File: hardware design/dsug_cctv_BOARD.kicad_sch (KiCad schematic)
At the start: 54 parts, among them J1 Conn_02x05_Top_Bottom, J3 TYPEC-304-ACP16, SW1 TS-1187A-B-A-B, SW2 24_detent, SW3 SW_Push, U1 AMS1117-3.3, U13 RP2040, U15 AP63205WU, U16 74AHCT1G125, U2 W25Q128JVS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

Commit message: minor pcb changes
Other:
- moved on the sheet: C56
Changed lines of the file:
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@@
 	)
 	(junction
-		(at 80.01 257.81)
-		(diameter 0)
-		(color 0 0 0 0)
-	)
-	(junction
 		(at 364.236 207.264)
 		(diameter 0)
@@
 	)
 	(junction
-		(at 93.98 270.51)
-		(diameter 0)
-		(color 0 0 0 0)
-	)
-	(junction
 		(at 167.132 258.826)
 		(diameter 0)
@@
 	(wire
 		(pts
-			(xy 80.01 267.97) (xy 80.01 270.51)
+			(xy 242.57 107.188) (xy 230.632 107.188)
 		)
 		(stroke
@@
 	(wire
 		(pts
-			(xy 242.57 107.188) (xy 230.632 107.188)
+			(xy 135.89 200.66) (xy 123.19 200.66)
 		)
 		(stroke
@@
 	(wire
 		(pts
-			(xy 80.01 270.51) (xy 93.98 270.51)
-		)
-		(stroke
-			(width 0)
-			(type default)
-		)
-	)
-	(wire
-		(pts
 			(xy 293.624 211.328) (xy 293.624 209.296)
 		)
@@
 	(wire
 		(pts
+			(xy 135.89 203.2) (xy 135.89 200.66)
+		)
+		(stroke
+			(width 0)
+			(type default)
+		)
+	)
+	(wire
+		(pts
 			(xy 341.376 184.912) (xy 339.598 184.912)
 		)
@@
 	(wire
 		(pts
+			(xy 135.89 214.63) (xy 135.89 210.82)
+		)
+		(stroke
+			(width 0)
+			(type default)
+		)
+	)
+	(wire
+		(pts
 			(xy 143.51 258.826) (xy 155.702 258.826)
 		)
@@
 	(wire
 		(pts
-			(xy 80.01 257.81) (xy 80.01 260.35)
-		)
-		(stroke
-			(width 0)
-			(type default)
-		)
-	)
-	(wire
-		(pts
 			(xy 118.11 200.66) (xy 115.57 200.66)
 		)
@@
 	(symbol
 		(lib_id "Device:C_Polarized_US")
-		(at 80.01 264.16 0)
+		(at 135.89 207.01 0)
 		(unit 1)
 		(exclude_from_sim no)
@@
 		(fields_autoplaced yes)
 		(property "Reference" "C56"
-			(at 83.82 262.2549 0)
+			(at 139.7 205.1049 0)
 			(effects
 				(font
@@
 		)
 		(property "Value" "22uF"
-			(at 83.82 264.7949 0)
+			(at 139.7 207.6449 0)
 			(effects
 				(font
@@
 		)
 		(property "Footprint" "Capacitor_THT:CP_Radial_D5.0mm_P2.50mm"
-			(at 80.01 264.16 0)
+			(at 135.89 207.01 0)
 			(effects
 				(font
@@
 		)
 		(property "Datasheet" "~"
-			(at 80.01 264.16 0)
+			(at 135.89 207.01 0)
 			(effects
 				(font
@@
 		)
 		(property "Description" ""
-			(at 80.01 264.16 0)
+			(at 135.89 207.01 0)
 			(effects
 				(font
@@
 					(unit 1)
 				)
+			)
+		)
+	)
+	(symbol
+		(lib_name "GND_1")
+		(lib_id "power:GND")
+		(at 135.89 214.63 0)
+		(unit 1)
+		(exclude_from_sim no)
+		(in_bom yes)
+		(on_board yes)
+		(dnp no)
+		(fields_autoplaced yes)
+		(property "Reference" "#PWR076"
+			(at 135.89 220.98 0)
+			(effects
+				(font
+					(size 1.27 1.27)
+				)
+				(hide yes)
+			)
+		)
+		(property "Value" "GND"
+			(at 135.89 219.71 0)
+			(effects
+				(font
+					(size 1.27 1.27)
+				)
+			)
+		)
+		(property "Footprint" ""
+			(at 135.89 214.63 0)
+			(effects
+				(font
+					(size 1.27 1.27)
+				)
+				(hide yes)
+			)
+		)
+		(property "Datasheet" ""
+			(at 135.89 214.63 0)
+			(effects
+				(font
+					(size 1.27 1.27)
+				)
+				(hide yes)
+			)
+		)
+		(property "Description" "Power symbol creates a global label with name \"GND\" , ground"
+			(at 135.89 214.63 0)
+			(effects
+				(font
+					(size 1.27 1.27)
+				)
+				(hide yes)
+			)
+		)
+		(pin "1"
+		)
+		(instances
+			(project "dsug_cctv_BOARD"
+				(path "/51d56f2e-5cbb-4b7a-b5cc-91fdc3a7308d"
+					(reference "#PWR076")
+					(unit 1)
+				)

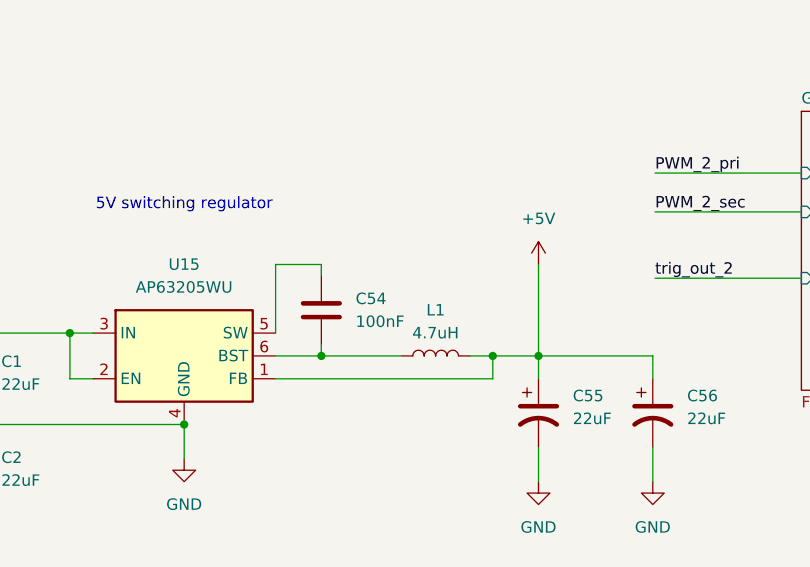
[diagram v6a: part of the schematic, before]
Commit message: switched pin that inductor on buck recitifier is connected to
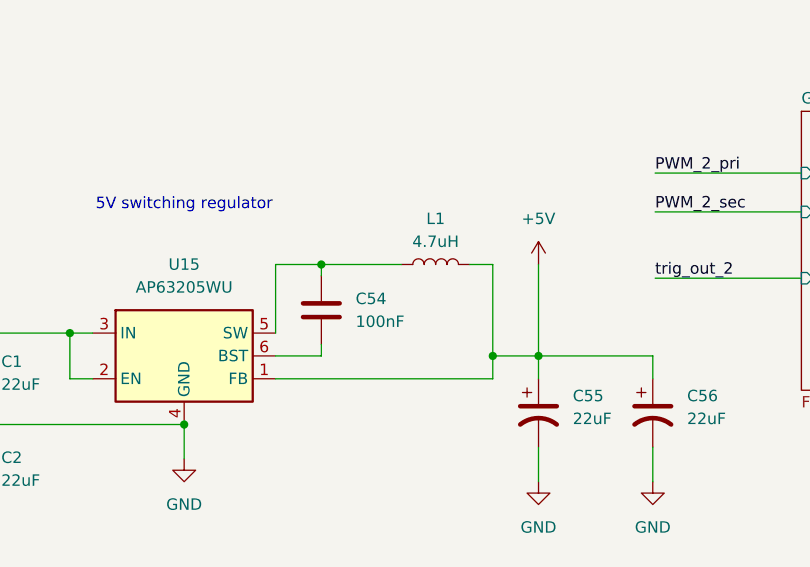
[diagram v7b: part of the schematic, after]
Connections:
- net at C54.1, U15.5 (SW): now also L1.1
- net at C54.2, U15.6 (BST): no longer L1.1
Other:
- moved on the sheet: L1
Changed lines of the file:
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@@
 	)
 	(junction
-		(at 99.06 200.66)
-		(diameter 0)
-		(color 0 0 0 0)
-	)
-	(junction
 		(at 199.898 258.826)
 		(diameter 0)
@@
 	)
 	(junction
+		(at 99.06 190.5)
+		(diameter 0)
+		(color 0 0 0 0)
+	)
+	(junction
 		(at 107.95 257.81)
 		(diameter 0)
@@
 	(wire
 		(pts
-			(xy 99.06 190.5) (xy 99.06 191.77)
-		)
-		(stroke
-			(width 0)
-			(type default)
-		)
-	)
-	(wire
-		(pts
 			(xy 198.374 60.452) (xy 199.898 60.452)
 		)
@@
 	(wire
 		(pts
+			(xy 99.06 199.39) (xy 99.06 200.66)
+		)
+		(stroke
+			(width 0)
+			(type default)
+		)
+	)
+	(wire
+		(pts
 			(xy 135.89 203.2) (xy 135.89 200.66)
 		)
@@
 	(wire
 		(pts
-			(xy 99.06 200.66) (xy 107.95 200.66)
+			(xy 99.06 190.5) (xy 107.95 190.5)
 		)
 		(stroke
@@
 	(wire
 		(pts
+			(xy 118.11 190.5) (xy 118.11 200.66)
+		)
+		(stroke
+			(width 0)
+			(type default)
+		)
+	)
+	(wire
+		(pts
 			(xy 184.912 175.006) (xy 205.232 175.006)
 		)
@@
 	(wire
 		(pts
-			(xy 99.06 199.39) (xy 99.06 200.66)
-		)
-		(stroke
-			(width 0)
-			(type default)
-		)
-	)
-	(wire
-		(pts
 			(xy 323.342 174.752) (xy 315.214 174.752)
 		)
@@
 	(wire
 		(pts
-			(xy 118.11 200.66) (xy 115.57 200.66)
+			(xy 118.11 190.5) (xy 115.57 190.5)
 		)
 		(stroke
@@
 	(wire
 		(pts
+			(xy 99.06 190.5) (xy 99.06 191.77)
+		)
+		(stroke
+			(width 0)
+			(type default)
+		)
+	)
+	(wire
+		(pts
 			(xy 242.57 167.386) (xy 230.632 167.386)
 		)
@@
 	(symbol
 		(lib_id "Device:L")
-		(at 111.76 200.66 90)
+		(at 111.76 190.5 90)
 		(unit 1)
 		(exclude_from_sim no)
@@
 		(fields_autoplaced yes)
 		(property "Reference" "L1"
-			(at 111.76 195.58 90)
+			(at 111.76 185.42 90)
 			(effects
 				(font
@@
 		)
 		(property "Value" "4.7uH"
-			(at 111.76 198.12 90)
+			(at 111.76 187.96 90)
 			(effects
 				(font
@@
 		)
 		(property "Footprint" "User_Footprints:L_TaiTech_HPC3010TF-4R7M"
-			(at 111.76 200.66 0)
+			(at 111.76 190.5 0)
 			(effects
 				(font
@@
 		)
 		(property "Datasheet" "~"
-			(at 111.76 200.66 0)
+			(at 111.76 190.5 0)
 			(effects
 				(font
@@
 		)
 		(property "Description" "Inductor"
-			(at 111.76 200.66 0)
+			(at 111.76 190.5 0)
 			(effects
 				(font

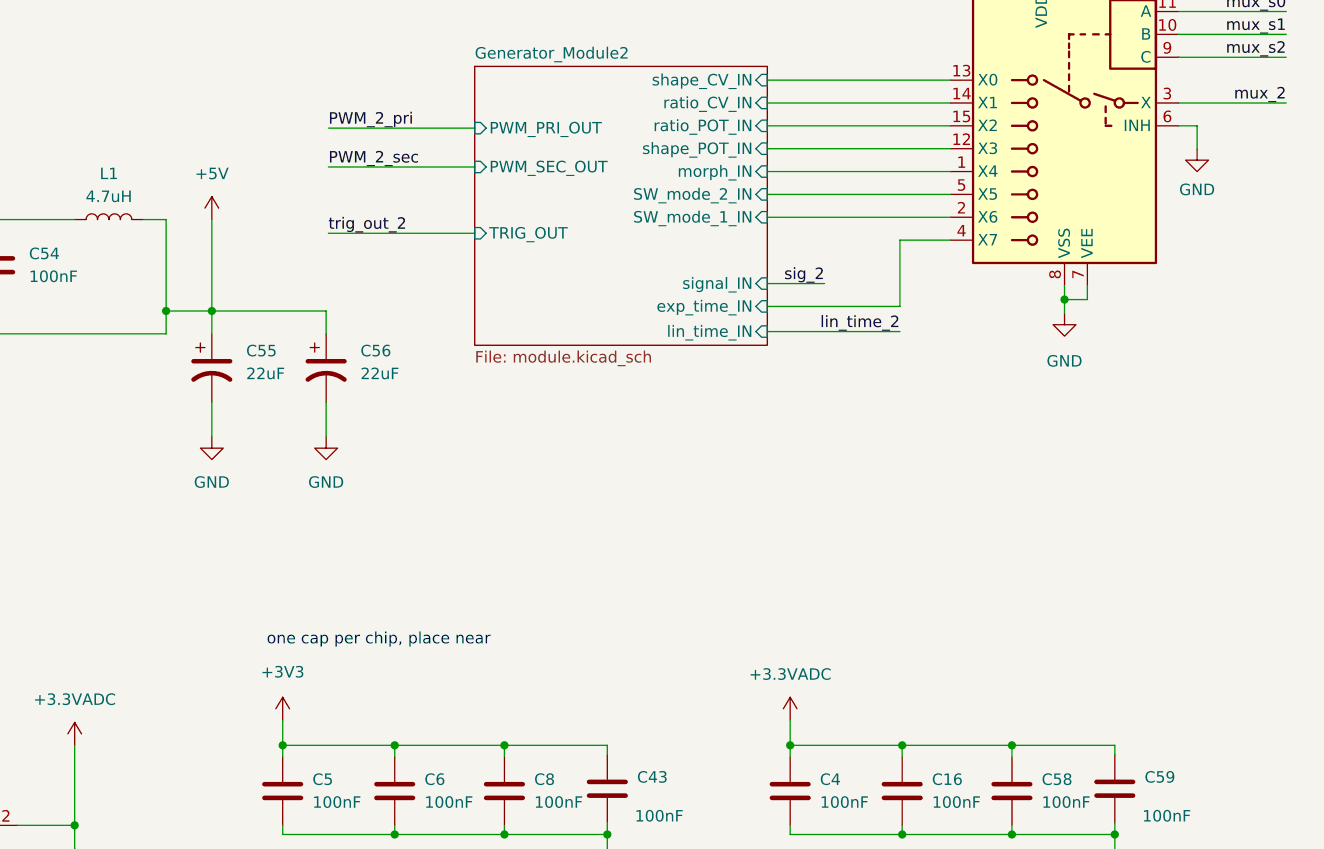
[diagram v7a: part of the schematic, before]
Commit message: added four more decoupling caps
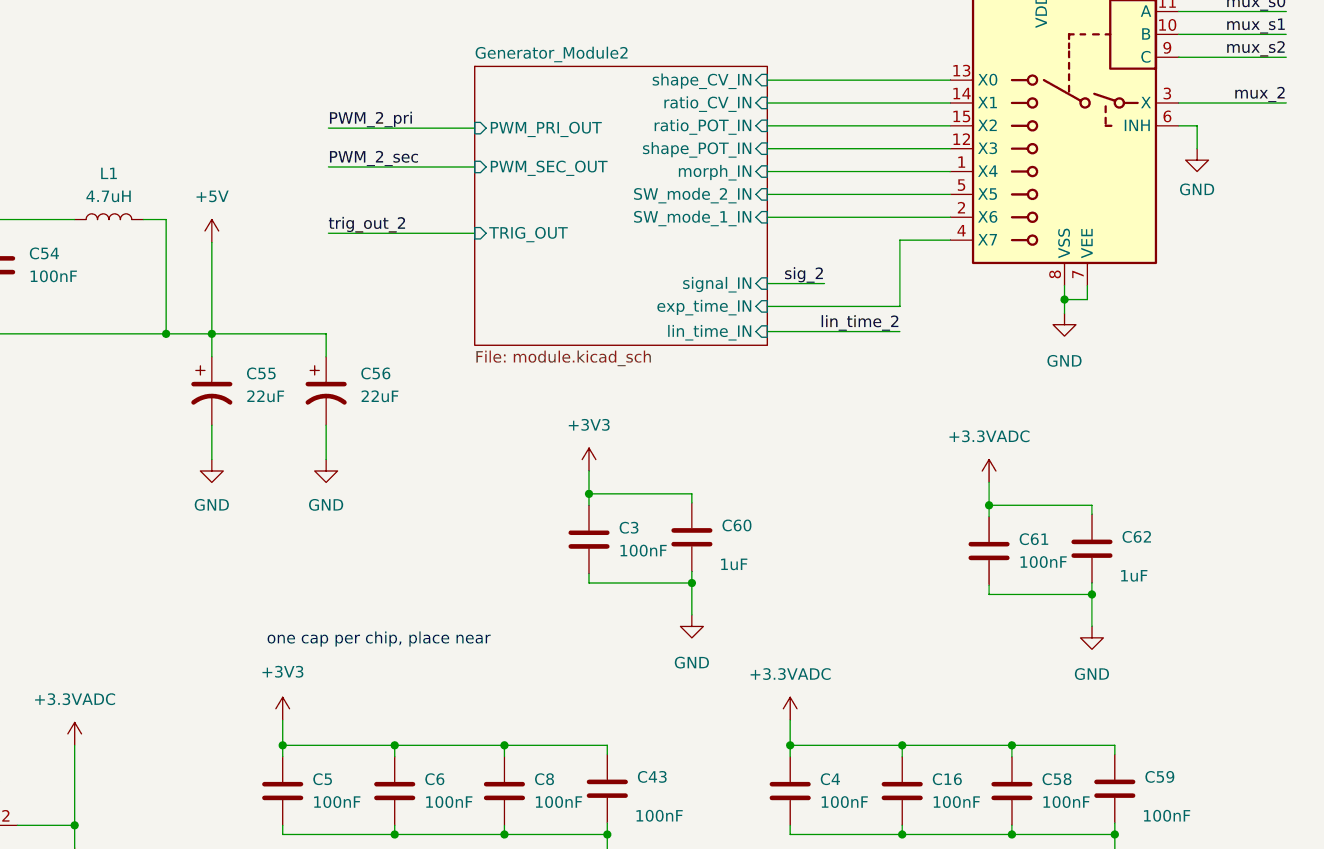
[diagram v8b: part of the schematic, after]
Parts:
- added C3, C61: 100nF, Capacitor_SMD:C_0603_1608Metric, symbol Device:C
- added C60, C62: 1uF, Capacitor_SMD:C_0603_1608Metric, symbol Device:C
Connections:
- net +3.3VADC: now also C61.1, C62.1
- net +3V3: now also C3.1, C60.1
- net GND: now also C3.2, C60.2, C61.2, C62.2
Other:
- moved on the sheet: C55, C56
